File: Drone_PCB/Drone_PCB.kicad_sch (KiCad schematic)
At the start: 58 parts, among them J1 Conn_01x04_Pin, J2 Conn_01x08_Socket, J3 Conn_01x05_Socket, J4 Conn_01x02_Socket, J5 Conn_01x02_Socket, J6 Conn_01x02_Socket, J7 Conn_01x02_Socket, J8 USB_B_Micro, Q1 AO3400A, Q2 AO3400A, Q3 AO3400A, Q4 AO3400A, Q5 AO3400A, Q6 AO3400A, SW1 SW_MEC_5G, SW2 SW_DPST_x2, U1 STM32F411RCT6, U2 AP2112K-3.3, U3 TP4056-42-ESOP8, U4 DW01A, Y1 26MHz

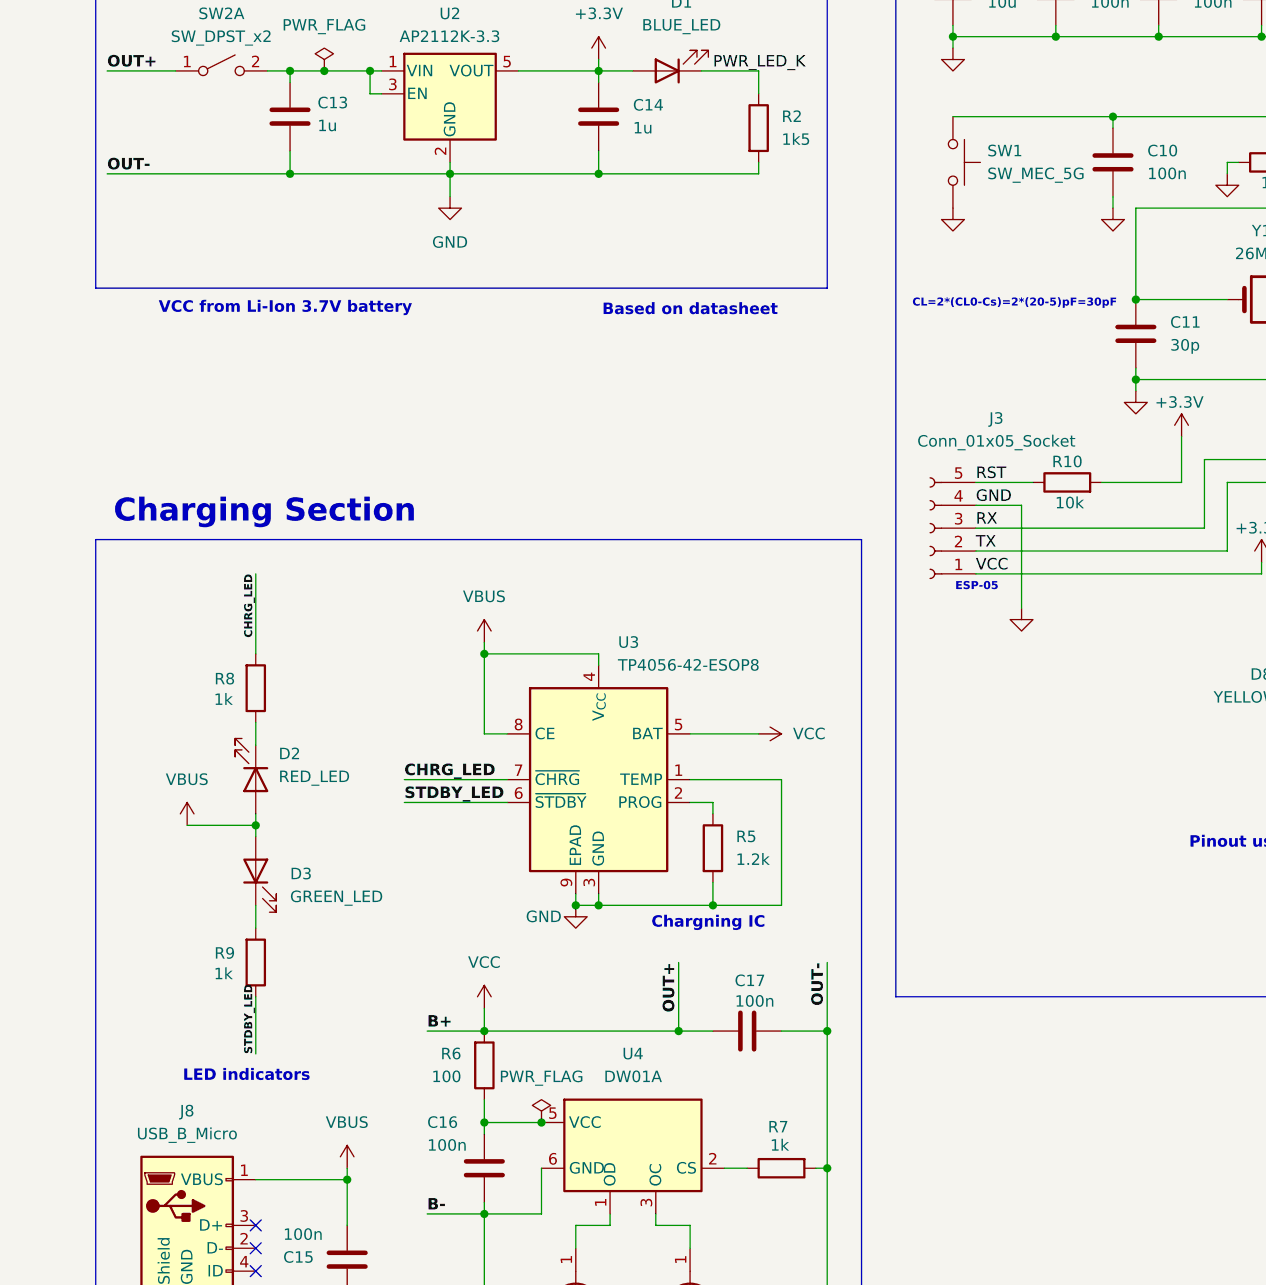
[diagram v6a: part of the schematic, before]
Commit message: Battery output + changing few things
Absolutely forgot about power source socket ( battery )
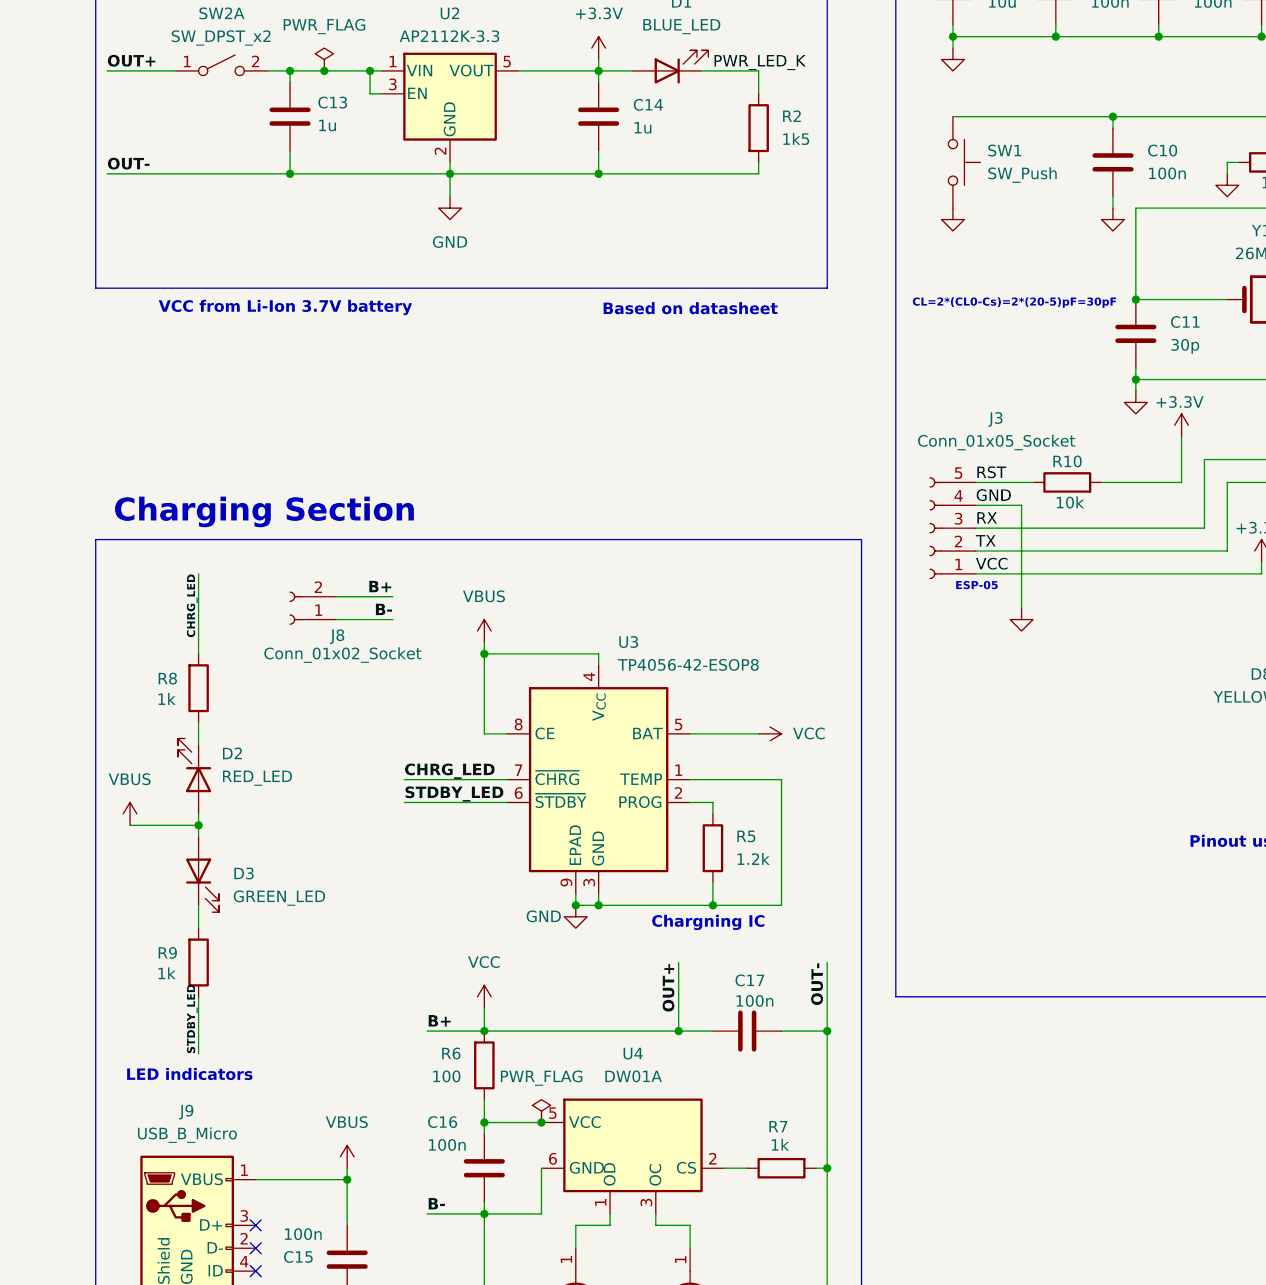
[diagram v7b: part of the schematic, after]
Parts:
- removed SW1: SW_MEC_5G, symbol Switch:SW_MEC_5G
- added J8: Conn_01x02_Socket, Connector_PinSocket_2.54mm:PinSocket_1x02_P2.54mm_Vertical, symbol Connector:Conn_01x02_Socket
- added SW1: SW_Push, Button_Switch_THT:SW_PUSH_6mm, symbol Switch:SW_Push
- D8: footprint (none) -> LED_SMD:LED_0603_1608Metric
- J2: footprint (none) -> Connector_PinSocket_2.54mm:PinSocket_1x08_P2.54mm_Vertical
- J3: footprint (none) -> Connector_PinSocket_2.54mm:PinSocket_1x05_P2.54mm_Vertical
- J4, J5, J6, J7: footprint (none) -> Connector_PinSocket_2.54mm:PinSocket_1x02_P2.54mm_Vertical
- renumbered J8 to J9
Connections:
- net +3.3V: now also J8.2 (Pin_2)
- net GND: now also J8.1 (Pin_1), SW1.2
- net NRST: now also SW1.1
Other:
- moved on the sheet: D2, D3, R8, R9

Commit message: Chose elements
I guess it's all of them
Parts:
- removed SW2: SW_DPST_x2, Button_Switch_THT:SW_E-Switch_EG1224_SPDT_Angled, symbol Switch:SW_DPST_x2
- added SW2: SW_SPST, Button_Switch_SMD:SW_DIP_SPSTx01_Slide_6.7x4.1mm_W6.73mm_P2.54mm_LowProfile_JPin, symbol Switch:SW_SPST
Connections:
- net +3.3V: now also SW2.1 (A)
- net at C13.1, U2.1 (VIN), U2.3 (EN): now also SW2.2 (B)
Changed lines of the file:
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@@
+	)
+	(symbol
+		(lib_id "Switch:SW_SPST")
+		(at 31.75 45.72 0)
+		(unit 1)
+		(exclude_from_sim no)
+		(in_bom yes)
+		(on_board yes)
+		(dnp no)
+		(fields_autoplaced yes)
+		(property "Reference" "SW2"
+			(at 31.75 39.37 0)
+			(effects
+				(font
+					(size 1.27 1.27)
+				)
+			)
+		)
+		(property "Value" "SW_SPST"
+			(at 31.75 41.91 0)
+			(effects
+				(font
+					(size 1.27 1.27)
+				)
+			)
+		)
+		(property "Footprint" "Button_Switch_SMD:SW_DIP_SPSTx01_Slide_6.7x4.1mm_W6.73mm_P2.54mm_LowProfile_JPin"
+			(at 31.75 45.72 0)
+			(effects
+				(font
+					(size 1.27 1.27)
+				)
+				(hide yes)
+			)
+		)
+		(property "Datasheet" "~"
+			(at 31.75 45.72 0)
+			(effects
+				(font
+					(size 1.27 1.27)
+				)
+				(hide yes)
+			)
+		)
+		(property "Description" "Single Pole Single Throw (SPST) switch"
+			(at 31.75 45.72 0)
+			(effects
+				(font
+					(size 1.27 1.27)
+				)
+				(hide yes)
+			)
+		)
+		(pin "2"
+		)
+		(pin "1"
+		)
+		(instances
+			(project ""
+				(path "/2c198202-91eb-4035-8605-360d42f3c3f5"
+					(reference "SW2")
+					(unit 1)
+				)
+			)
+		)
 	)
 	(symbol
@@
 					(unit 1)
 				)
-			)
-		)
-	)
-	(symbol
-		(lib_id "Switch:SW_DPST_x2")
-		(at 31.75 45.72 0)
-		(unit 1)
-		(exclude_from_sim no)
-		(in_bom yes)
-		(on_board yes)
-		(dnp no)
-		(fields_autoplaced yes)
-		(property "Reference" "SW2"
-			(at 31.75 39.37 0)
-			(effects
-				(font
-					(size 1.27 1.27)
-				)
-			)
-		)
-		(property "Value" "SW_DPST_x2"
-			(at 31.75 41.91 0)
-			(effects
-				(font
-					(size 1.27 1.27)
-				)
-			)
-		)
-		(property "Footprint" "Button_Switch_THT:SW_E-Switch_EG1224_SPDT_Angled"
-			(at 31.75 45.72 0)
-			(effects
-				(font
-					(size 1.27 1.27)
-				)
-				(hide yes)
-			)
-		)
-		(property "Datasheet" "~"
-			(at 31.75 45.72 0)
-			(effects
-				(font
-					(size 1.27 1.27)
-				)
-				(hide yes)
-			)
-		)
-		(property "Description" "Single Pole Single Throw (SPST) switch, separate symbol"
-			(at 31.75 45.72 0)
-			(effects
-				(font
-					(size 1.27 1.27)
-				)
-				(hide yes)
-			)
-		)
-		(pin "4"
-		)
-		(pin "1"
-		)
-		(pin "2"
-		)
-		(pin "3"
-		)
-		(instances
-			(project "Drone_PCB"
-				(path "/2c198202-91eb-4035-8605-360d42f3c3f5"
-					(reference "SW2")
-					(unit 1)
-				)
